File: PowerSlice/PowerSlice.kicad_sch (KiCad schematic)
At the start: 33 parts, among them J1 Conn_01x08_Pin, J2 DC_In_Barrel, J3 DC_In_Screw, J4 ESTOP, U1 PTH08080WAD, U2 PTH08080WAD, U3 INA214BIDCKR, U4 INA214BIDCKR, U5 INA214BIDCKR, U6 NUCLEO-F303K8

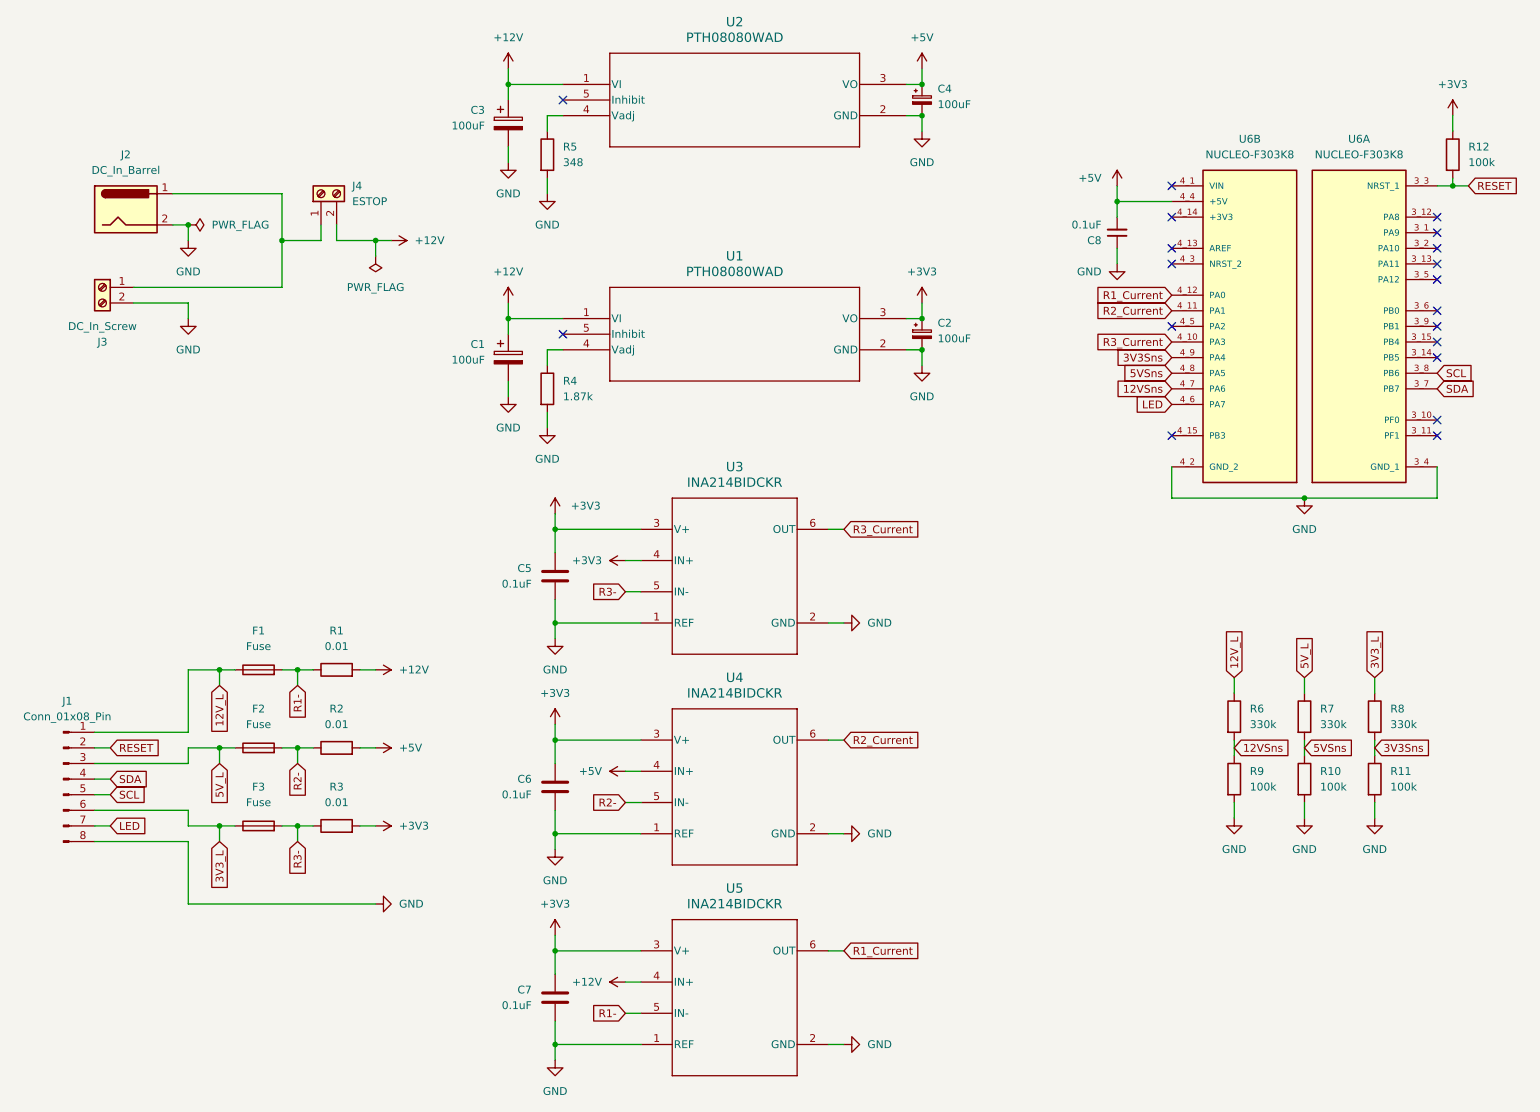
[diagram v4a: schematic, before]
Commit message: Updated schematic + built PCB
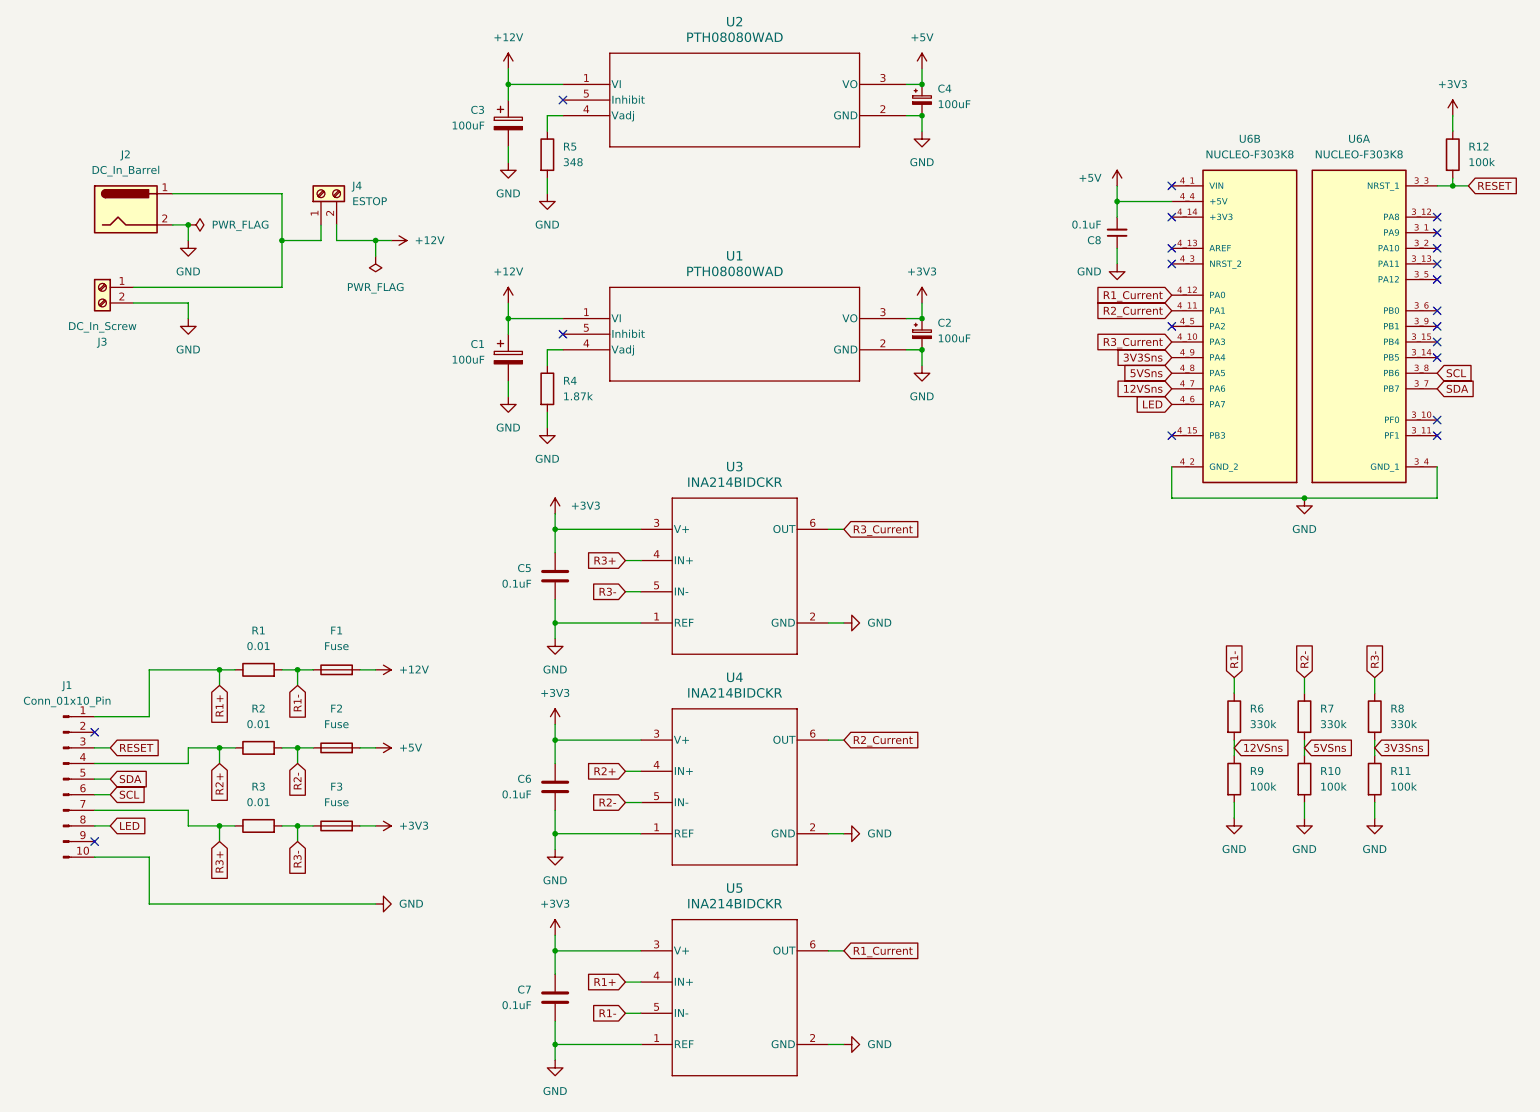
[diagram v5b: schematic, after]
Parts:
- removed J1: Conn_01x08_Pin, symbol Connector:Conn_01x08_Pin
- added J1: Conn_01x10_Pin, Connector_PinHeader_2.54mm:PinHeader_1x10_P2.54mm_Horizontal, symbol Connector:Conn_01x10_Pin
- C1, C2, C3, C4: footprint (none) -> Capacitor_THT:CP_Radial_D6.3mm_P2.50mm
- C5, C6, C7, C8: footprint (none) -> Capacitor_SMD:C_1206_3216Metric_Pad1.33x1.80mm_HandSolder
- J3, J4: footprint (none) -> 691137710002:691137710002
- R1, R10, R11, R12, R2, R3, R4, R5, R6, R7, R8, R9: footprint (none) -> Resistor_SMD:R_1206_3216Metric_Pad1.30x1.75mm_HandSolder
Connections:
- net 12V_L is gone; now on net R1-: F1.1, R6.1
- net 3V3_L is gone; now on net R3-: F3.1, R8.1
- net 5V_L is gone; now on net R2-: F2.1, R7.1
- net +12V: now also F1.2; no longer R1.2, U5.4 (IN+)
- net +3V3: now also F3.2; no longer R3.2, U3.4 (IN+)
- net +5V: now also F2.2; no longer R2.2, U4.4 (IN+)
- net GND: now also J1.10 (Pin_10)
- net LED: now also J1.8 (Pin_8)
- net R1-: now also R1.2; no longer F1.2, R1.1
- net R2-: now also R2.2; no longer F2.2, R2.1
- net R3-: now also R3.2; no longer F3.2, R3.1
- net RESET: now also J1.3 (Pin_3)
- net SCL: now also J1.6 (Pin_6)
- net SDA: now also J1.5 (Pin_5)
- new net R1+: J1.1 (Pin_1), R1.1, U5.4 (IN+)
- new net R2+: J1.4 (Pin_4), R2.1, U4.4 (IN+)
- new net R3+: J1.7 (Pin_7), R3.1, U3.4 (IN+)
- no-connect marks 19 -> 21
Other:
- moved on the sheet: F1, F2, F3, R1, R2, R3

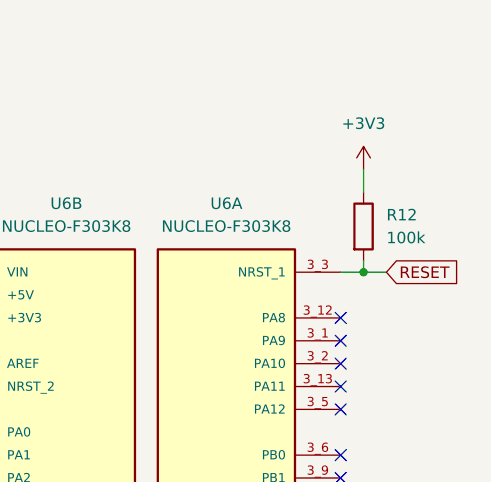
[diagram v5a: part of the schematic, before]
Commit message: updated lightly after PCB review TODO: figure out LED and Header pins
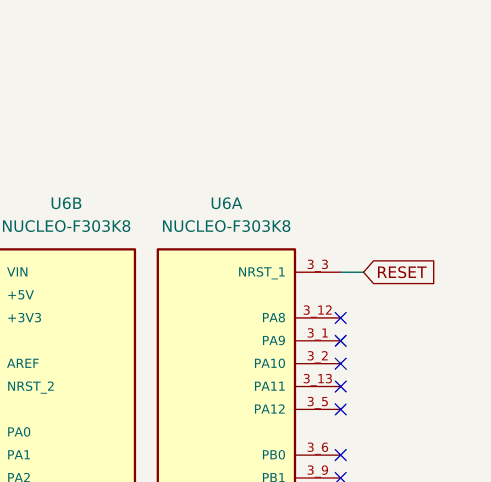
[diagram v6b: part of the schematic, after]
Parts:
- removed R12: 100k, Resistor_SMD:R_1206_3216Metric_Pad1.30x1.75mm_HandSolder, symbol Device:R
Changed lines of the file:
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@@
 	)
 	(junction
-		(at 250.19 43.18)
-		(diameter 0)
-		(color 0 0 0 0)
-	)
-	(junction
 		(at 62.23 134.62)
 		(diameter 0)
@@
 	(wire
 		(pts
-			(xy 250.19 31.75) (xy 250.19 34.29)
-		)
-		(stroke
-			(width 0)
-			(type default)
-		)
-	)
-	(wire
-		(pts
 			(xy 62.23 121.92) (xy 62.23 124.46)
 		)
@@
 	(wire
 		(pts
-			(xy 250.19 43.18) (xy 252.73 43.18)
-		)
-		(stroke
-			(width 0)
-			(type default)
-		)
-	)
-	(wire
-		(pts
 			(xy 96.52 36.83) (xy 96.52 39.37)
 		)
@@
 	(wire
 		(pts
-			(xy 250.19 43.18) (xy 250.19 41.91)
-		)
-		(stroke
-			(width 0)
-			(type default)
-		)
-	)
-	(wire
-		(pts
 			(xy 59.69 147.32) (xy 62.23 147.32)
 		)
@@
 	(global_label "RESET"
 		(shape input)
-		(at 252.73 43.18 0)
+		(at 250.19 43.18 0)
 		(fields_autoplaced yes)
 		(effects
@@
 		)
 		(property "Intersheetrefs" "${INTERSHEET_REFS}"
-			(at 261.4603 43.18 0)
+			(at 258.9203 43.18 0)
 			(effects
 				(font
@@
 	)
 	(symbol
-		(lib_id "Device:R")
-		(at 250.19 38.1 0)
-		(unit 1)
-		(exclude_from_sim no)
-		(in_bom yes)
-		(on_board yes)
-		(dnp no)
-		(fields_autoplaced yes)
-		(property "Reference" "R12"
-			(at 252.73 36.8299 0)
-			(effects
-				(font
-					(size 1.27 1.27)
-				)
-				(justify left)
-			)
-		)
-		(property "Value" "100k"
-			(at 252.73 39.3699 0)
-			(effects
-				(font
-					(size 1.27 1.27)
-				)
-				(justify left)
-			)
-		)
-		(property "Footprint" "Resistor_SMD:R_1206_3216Metric_Pad1.30x1.75mm_HandSolder"
-			(at 248.412 38.1 90)
-			(effects
-				(font
-					(size 1.27 1.27)
-				)
-				(hide yes)
-			)
-		)
-		(property "Datasheet" "~"
-			(at 250.19 38.1 0)
-			(effects
-				(font
-					(size 1.27 1.27)
-				)
-				(hide yes)
-			)
-		)
-		(property "Description" "Resistor"
-			(at 250.19 38.1 0)
-			(effects
-				(font
-					(size 1.27 1.27)
-				)
-				(hide yes)
-			)
-		)
-		(pin "2"
-		)
-		(pin "1"
-		)
-		(instances
-			(project ""
-				(path "/871cf238-4ac7-4d02-abe8-ea643d22c598"
-					(reference "R12")
-					(unit 1)
-				)
-			)
-		)
-	)
-	(symbol
 		(lib_id "power:PWR_FLAG")
 		(at 44.45 49.53 270)
@@
 					(unit 1)
 				)
-			)
-		)
-	)
-	(symbol
-		(lib_id "power:+3V3")
-		(at 250.19 31.75 0)
-		(unit 1)
-		(exclude_from_sim no)
-		(in_bom yes)
-		(on_board yes)
-		(dnp no)
-		(fields_autoplaced yes)
-		(property "Reference" "#PWR033"
-			(at 250.19 35.56 0)
-			(effects
-				(font
-					(size 1.27 1.27)
-				)
-				(hide yes)
-			)
-		)
-		(property "Value" "+3V3"
-			(at 250.19 26.67 0)
-			(effects
-				(font
-					(size 1.27 1.27)
-				)
-			)
-		)
-		(property "Footprint" ""
-			(at 250.19 31.75 0)
-			(effects
-				(font
-					(size 1.27 1.27)
-				)
-				(hide yes)
-			)
-		)
-		(property "Datasheet" ""
-			(at 250.19 31.75 0)
-			(effects
-				(font
-					(size 1.27 1.27)
-				)
-				(hide yes)
-			)
-		)
-		(property "Description" "Power symbol creates a global label with name \"+3V3\""
-			(at 250.19 31.75 0)
-			(effects
-				(font
-					(size 1.27 1.27)
-				)
-				(hide yes)
-			)
-		)
-		(pin "1"
-		)
-		(instances
-			(project ""
-				(path "/871cf238-4ac7-4d02-abe8-ea643d22c598"
-					(reference "#PWR033")
-					(unit 1)
-				)

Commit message: Wacky stuff that needs to be changed cuz it wont work and will be reverted
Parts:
- added J5: +12V_Screw, 691137710002:691137710002, symbol Connector:Screw_Terminal_01x02
- added J6: +5V_Screw, 691137710002:691137710002, symbol Connector:Screw_Terminal_01x02
- added J7: +3V3_Screw, 691137710002:691137710002, symbol Connector:Screw_Terminal_01x02
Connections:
- net GND: now also J1.8 (Pin_8), J5.2 (Pin_2), J6.2 (Pin_2), J7.2 (Pin_2)
- net LED: now also J1.7 (Pin_7); no longer J1.8 (Pin_8)
- net RESET: now also J1.2 (Pin_2); no longer J1.3 (Pin_3)
- net SCL: now also J1.5 (Pin_5); no longer J1.6 (Pin_6)
- net SDA: now also J1.4 (Pin_4); no longer J1.5 (Pin_5)
- net E_STOP: now reaches J1.9 (Pin_9)
- net E_STOP: now also U6.3_14 (PB5)
- net R1+ renamed +12V_L
- net +12V_L: now also J5.1 (Pin_1)
- net R2+ renamed +5V_L
- net +5V_L: now also J1.6 (Pin_6), J6.1 (Pin_1); no longer J1.4 (Pin_4)
- net R3+ renamed +3V3_L
- net +3V3_L: now also J1.3 (Pin_3), J7.1 (Pin_1); no longer J1.7 (Pin_7)
- no-connect marks 21 -> 18
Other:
- moved on the sheet: C8, F1, F2, F3, J1, R1, R2, R3, R6, R9

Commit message: Work, TODO: figure out external power connectors
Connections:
- net +3V3_L: now also J1.6 (Pin_6); no longer J1.3 (Pin_3)
- net +5V_L: now also J1.3 (Pin_3); no longer J1.6 (Pin_6)
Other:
- moved on the sheet: C5, C6, C7
